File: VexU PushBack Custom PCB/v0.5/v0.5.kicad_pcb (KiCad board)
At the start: 2 copper layers, 40.5 x 70 mm, 40 parts, among them J1 4P4C, J2 Conn_01x04_Pin, U1 Teensy4.1, U2 MP2338GTL-P, U3 4069, U4 MAX485E

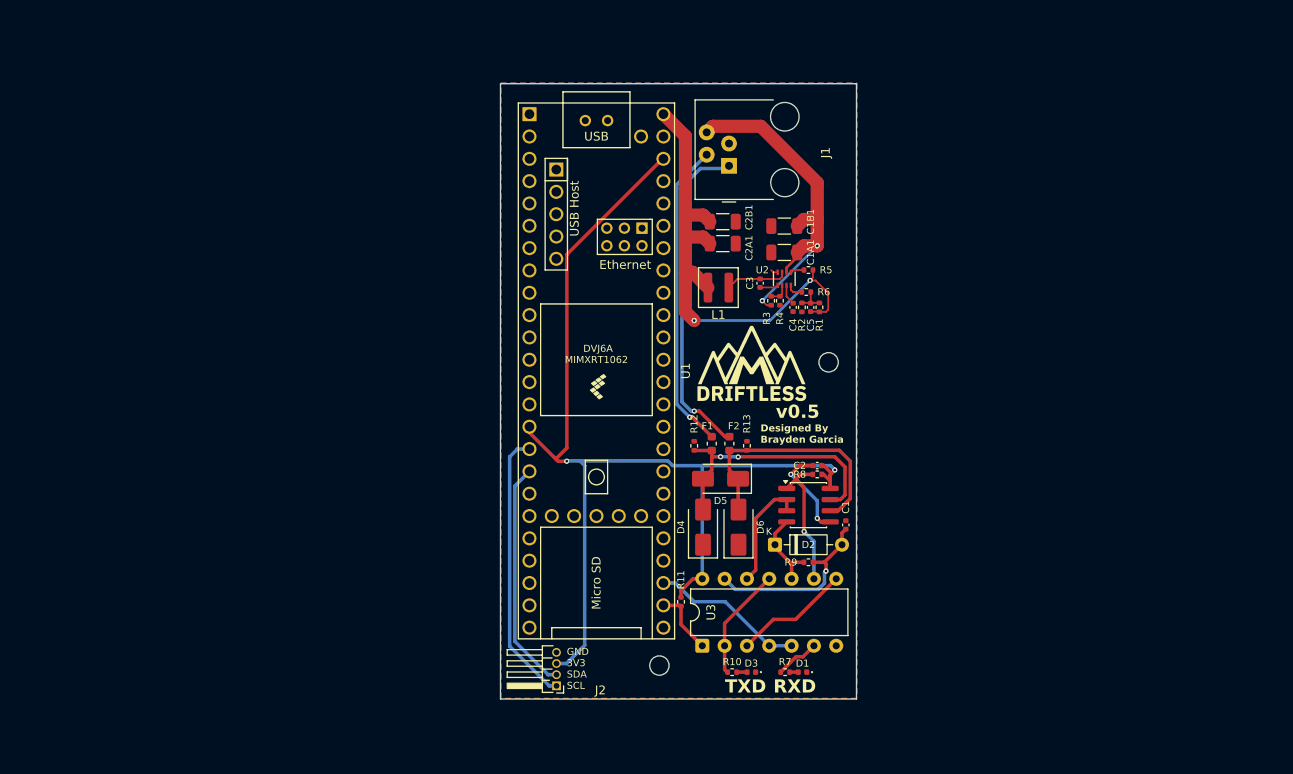
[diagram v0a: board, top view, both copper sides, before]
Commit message: Schematic fully done
will need to keep working on tracing and component layout
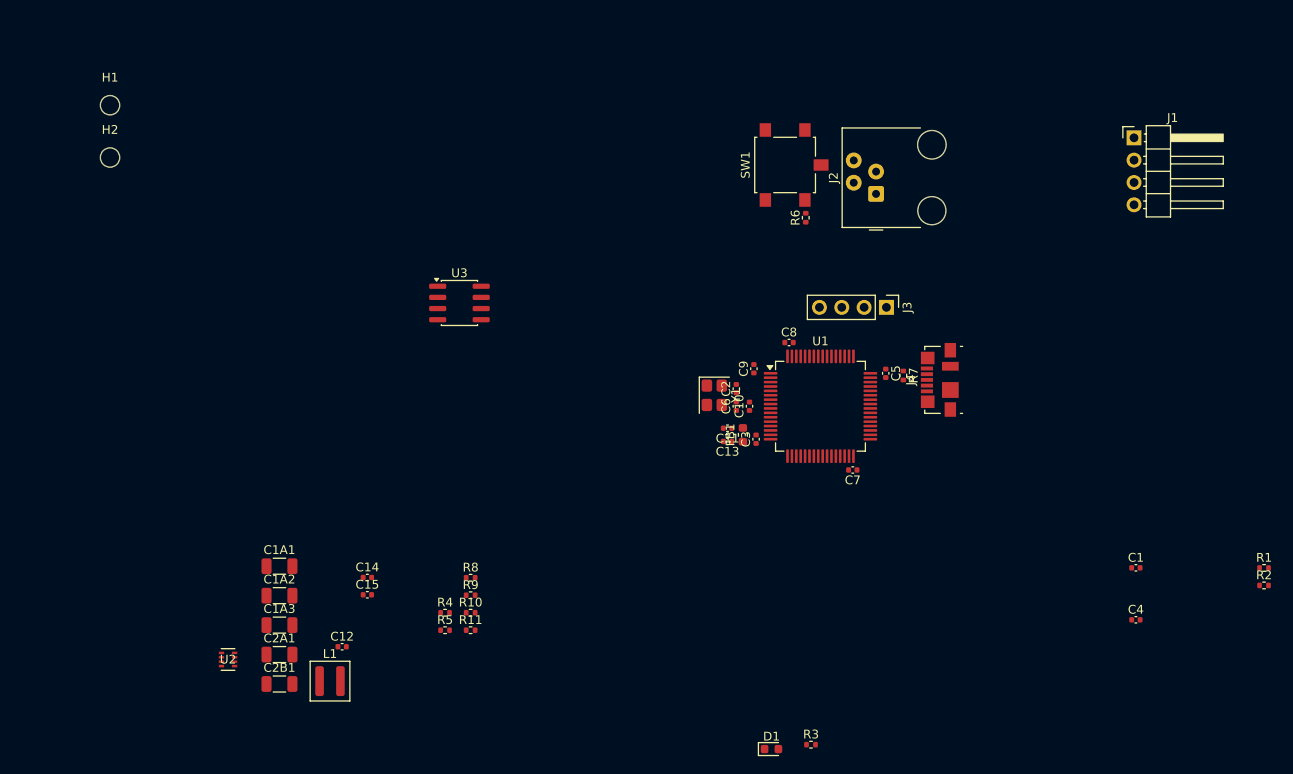
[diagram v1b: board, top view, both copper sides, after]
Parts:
- removed C1B1: 0.1μF, Capacitor_SMD:C_1206_3216Metric
- removed D2: 1N4148, Diode_THT:D_DO-35_SOD27_P7.62mm_Horizontal
- removed D3: TXD, LED_SMD:LED_0402_1005Metric
- removed D4, D5, D6: SMAJ6.5CA, Diode_SMD:D_SMA
- removed F1, F2: 0.3A, Fuse:Fuse_0603_1608Metric
- removed G***: LOGO, LOGO
- removed R12, R13: 4.7k, Resistor_SMD:R_0402_1005Metric
- removed U4: MAX485E, Package_SO:SOIC-8_3.9x4.9mm_P1.27mm
- added C10: 10n, Capacitor_SMD:C_0402_1005Metric, F.Cu at (113.5, 60.5)
- added C11: 1u, Capacitor_SMD:C_0402_1005Metric, F.Cu at (111.0, 63.0)
- added C12: 22nF, Capacitor_SMD:C_0402_1005Metric, F.Cu at (67.2, 87.9)
- added C13: 1u, Capacitor_SMD:C_0402_1005Metric, F.Cu at (111.0, 64.5)
- added C14: 0.1μF, Capacitor_SMD:C_0402_1005Metric, F.Cu at (70.0, 80.0)
- added C15: 470pF, Capacitor_SMD:C_0402_1005Metric, F.Cu at (70.0, 82.0)
- added C1A2: 10u, Capacitor_SMD:C_1206_3216Metric, F.Cu at (60.0, 82.0)
- added C1A3: 0.1μF, Capacitor_SMD:C_1206_3216Metric, F.Cu at (60.0, 85.4)
- added C6: 10p, Capacitor_SMD:C_0402_1005Metric, F.Cu at (112.0, 60.5)
- added C7: 100n, Capacitor_SMD:C_0402_1005Metric, F.Cu at (125.2, 67.8)
- added C8: 100n, Capacitor_SMD:C_0402_1005Metric, F.Cu at (118.0, 53.2)
- added C9: 100n, Capacitor_SMD:C_0402_1005Metric, F.Cu at (114.0, 56.2)
- added FB1: 120R, Inductor_SMD:L_0603_1608Metric, F.Cu at (112.8, 63.8)
- added J3: Conn_01x04_Pin, Connector_PinHeader_2.54mm:PinHeader_1x04_P2.54mm_Vertical, F.Cu at (129.1, 49.2)
- added J4: USB_B_Micro, Connector_USB:USB_Micro-B_Molex_47346-0001, F.Cu at (135.2, 57.5)
- added SW1: SW_SPDT, Button_Switch_SMD:SW_SPST_B3S-1100, F.Cu at (118.5, 33.0)
- added Y1: 16MHz, Crystal:Crystal_SMD_3225-4Pin_3.2x2.5mm, F.Cu at (109.5, 59.2)
- C1: value 100pF -> 10u
- C1A1: value 22μF -> 10u
- C2: value 0.1uF -> 10p
- C3: value 0.1μF -> 100n
- C4: value 22nF -> 100n
- C5: value 300pF -> 100n
- D1: value RXD -> RED; footprint LED_SMD:LED_0402_1005Metric -> LED_SMD:LED_0603_1608Metric
- J1: value 4P4C -> Conn_01x04_Pin; footprint Connector_RJ:RJ9_Evercom_5301-440xxx_Horizontal -> Connector_PinHeader_2.54mm:PinHeader_1x04_P2.54mm_Horizontal
- J2: value Conn_01x04_Pin -> 4P4C; footprint Connector_PinHeader_1.27mm:PinHeader_1x04_P1.27mm_Horizontal -> Connector_RJ:RJ9_Evercom_5301-440xxx_Horizontal
- R1: value 90.9kΩ -> 1.5k
- R10: value 2.4k -> 9.09kΩ
- R11: value 4.7k -> 51kΩ
- R2: value 10kΩ -> 1.5k
- R3: value 191kΩ -> 1.5k
- R4: value 49.9kΩ -> 191kΩ
- R5: value 10kΩ -> 49.9kΩ
- R6: value 10kΩ -> 10k
- R7: value 2.4k -> 1.5k
- R8: value 4.7k -> 100kΩ
- R9: value 56k -> 10kΩ
- U1: value Teensy4.1 -> STM32G431RBT6; footprint teensy.pretty-master:Teensy41 -> Package_QFP:LQFP-64_10x10mm_P0.5mm
- U3: value 4069 -> MAX485E; footprint Package_DIP:DIP-14_W7.62mm -> Package_SO:SOIC-8_3.9x4.9mm_P1.27mm
- moved H1 86.8 mm to (40.8, 26.2), turned to 0 degrees
- moved H2 85.1 mm to (40.8, 32.2), turned to 0 degrees
- moved U2 76.7 mm to (54.2, 89.3), turned to 0 degrees
- moved C2B1 72.9 mm to (60.0, 92.1)
- moved C2A1 68.8 mm to (60.0, 88.8)
- moved C1A1 67.6 mm to (60.0, 78.7), turned to 0 degrees
- moved J2 66.7 mm to (127.9, 36.3), turned to 90 degrees
- moved L1 62.9 mm to (65.8, 91.8), turned to 0 degrees
- moved R2 61.4 mm to (172.0, 80.9), turned to 0 degrees
- moved R1 58.6 mm to (172.0, 78.9), turned to 0 degrees
- moved R5 58.2 mm to (78.9, 86.0)
- moved C4 52.8 mm to (157.5, 84.8), turned to 0 degrees
- moved R4 52.1 mm to (78.9, 84.0), turned to 0 degrees
- moved R3 50.7 mm to (120.5, 99.0), turned to 0 degrees
- moved U3 47.8 mm to (80.5, 48.8), turned to 0 degrees
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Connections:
- C1 pad 1: Net-(D2-A) -> +3V3
- C1A1 pad 1: 12V -> VBUS
- C2 pad 1: 3V3 -> /HSE_IN
- C2A1 pad 1: 5V -> +3V3
- C2B1 pad 1: 5V -> +3V3
- C3 pad 1: Net-(U2-BST) -> +3V3
- C3 pad 2: Net-(U2-SW) -> GND
- C4 pad 1: Net-(U2-SS) -> /NRST
- C5 pad 1: Net-(C5-Pad1) -> +3V3
- C5 pad 2: 5V -> GND
- D1 pad 1: GND -> Net-(D1-K)
- D1 pad 2: Net-(D1-A) -> +3V3
- J1 pad 1: A -> GND
- J1 pad 2: B -> +3V3
- J1 pad 3: GND -> /I2C3_SDA
- J1 pad 4: 12V -> /I2C3_SCL
- J2 pad 1: SCL -> A
- J2 pad 2: SDA -> B
- J2 pad 3: 3V3 -> GND
- J2 pad 4: GND -> VBUS
- L1 pad 2: 5V -> +3V3
- R1 pad 1: Net-(C5-Pad1) -> +3V3
- R1 pad 2: 5V -> /I2C3_SDA
- R10 pad 1: Net-(R10-Pad1) -> GND
- R10 pad 2: Net-(D3-A) -> Net-(C15-Pad1)
- R11 pad 1: 3V3 -> Net-(C15-Pad1)
- R11 pad 2: RXD -> +3V3
- R2 pad 1: GND -> +3V3
- R2 pad 2: Net-(C5-Pad1) -> /I2C3_SCL
- R3 pad 1: 12V -> Net-(D1-K)
- R3 pad 2: Net-(U2-EN) -> GND
- R4 pad 1: Net-(U2-EN) -> VBUS
- R4 pad 2: GND -> Net-(U2-EN)
- R5 pad 1: Net-(U2-PG) -> Net-(U2-EN)
- R5 pad 2: 5V -> GND
- R6 pad 1: Net-(U2-FB) -> /BOOT0
- R6 pad 2: Net-(C5-Pad1) -> /SW_BOOT0
- R7 pad 1: Net-(R7-Pad1) -> +3V3
- R7 pad 2: Net-(D1-A) -> /USB_D+
- R8 pad 1: Net-(U4-RO) -> Net-(U2-PG)
- R8 pad 2: 3V3 -> +3V3
- R9 pad 1: Net-(D2-K) -> Net-(U2-FB)
- R9 pad 2: Net-(D2-A) -> Net-(C15-Pad1)
- U1 pad 1: GND -> +3V3
- U1 pad 15: 3V3 -> GND
- U1 pad 16: SCL -> +3V3
- U1 pad 17: SDA -> unconnected-(U1-PA3-Pad17)
- U1 pad 26: RXD -> unconnected-(U1-PB2-Pad26)
- U1 pad 27: TXD -> GND
- U1 pad 29: unconnected-(U1-37_CS-Pad29) -> +3.3VA
- U1 pad 31: unconnected-(U1-39_MISO1_OUT1A-Pad31) -> GND
- U1 pad 32: unconnected-(U1-40_A16-Pad32) -> +3V3
- U1 pad 34: GND -> unconnected-(U1-PB12-Pad34)
- U1 pad 40: unconnected-(U1-18_A4_SDA-Pad40) -> /I2C3_SCL
- U1 pad 41: unconnected-(U1-19_A5_SCL-Pad41) -> /I2C3_SDA
- U1 pad 45: unconnected-(U1-23_A9_CRX1_MCLK1-Pad45) -> /USB_D-
- U1 pad 46: 3V3 -> /USB_D+
- U1 pad 48: 5V -> +3V3
- U1 pad 49: unconnected-(U1-VUSB-Pad49) -> /SWDIO
- U1 pad 5: unconnected-(U1-3_LRCLK2-Pad5) -> /HSE_IN
- U1 pad 50: unconnected-(U1-VBAT-Pad50) -> /SWCLK
- U1 pad 58: unconnected-(U1-GND-Pad58) -> TX_EN
- U1 pad 59: unconnected-(U1-GND-Pad59) -> TXD
- U1 pad 6: unconnected-(U1-4_BCLK2-Pad6) -> /HSE_OUT
- U1 pad 60: unconnected-(U1-R+-Pad60) -> RXD
- U1 pad 61: unconnected-(U1-LED-Pad61) -> /BOOT0
- U1 pad 63: unconnected-(U1-T+-Pad63) -> GND
- U1 pad 64: unconnected-(U1-GND-Pad64) -> +3V3
- U1 pad 7: unconnected-(U1-5_IN2-Pad7) -> /NRST
- U2 pad 2: 12V -> VBUS
- U3 pad 2: Net-(R10-Pad1) -> TX_EN
- U3 pad 3: Net-(U3-Pad3) -> TX_EN
- U3 pad 5: TXD -> GND
- U3 pad 6: Net-(R7-Pad1) -> A
- U3 pad 7: GND -> B
- U3 pad 8: Net-(U3-Pad3) -> +3.3V
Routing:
- net 3V3: track 123.5 -> 0.00 mm, vias 2 -> 0
- net 5V: track 57.4 -> 0.00 mm, vias 2 -> 0
- net 12V: track 40.9 -> 0.00 mm, vias 2 -> 0
- net A: track 37.8 -> 0.00 mm, vias 1 -> 0
- net B: track 35.3 -> 0.00 mm, vias 1 -> 0
- net SCL: track 31.4 -> 0.00 mm
- net Net-(D4-A2): track 30.0 -> 0.00 mm, vias 2 -> 0
- net Net-(D5-A1): track 28.6 -> 0.00 mm
- net SDA: track 26.3 -> 0.00 mm
- net Net-(D2-A): track 20.8 -> 0.00 mm, vias 1 -> 0
- net TXD: track 17.5 -> 0.00 mm
- net Net-(U4-RO): track 15.8 -> 0.00 mm, vias 1 -> 0
- net Net-(U3-Pad3): track 13.3 -> 0.00 mm
- net Net-(U4-DE): track 13.0 -> 0.00 mm
- net Net-(R10-Pad1): track 12.9 -> 0.00 mm
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- removed copper zone on B.Cu, net GND
- removed copper zone on F.Cu, net GND
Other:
- board outline removed
- board text removed: "Designed By Brayden Garcia"
- board text removed: "GND 3V3 SDA SCL"
- board text removed: "RXD"
- board text removed: "TXD"
- board text removed: "v0.5"

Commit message: Layout of buck convertr
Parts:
- moved C4 130.9 mm to (32.4, 46.0), turned to 90 degrees
- moved C1 129.8 mm to (32.4, 44.0), turned to -90 degrees
- moved J1 94.6 mm to (66.0, 54.9)
- moved R3 80.9 mm to (77.5, 30.5), turned to 90 degrees
- moved D1 78.7 mm to (80.0, 29.5), turned to 180 degrees
- moved SW1 76.0 mm to (42.6, 37.5)
- moved H1 73.8 mm to (102.0, 67.5)
- moved H2 73.8 mm to (102.0, 73.5)
- moved R6 70.5 mm to (49.4, 38.5)
- moved C10 69.8 mm to (44.4, 50.5)
- moved C11 69.8 mm to (41.9, 53.0)
- moved C13 69.8 mm to (41.9, 54.5)
- moved C2 69.8 mm to (42.9, 48.5)
- moved C3 69.8 mm to (45.2, 54.2)
- moved C5 69.8 mm to (59.9, 46.8)
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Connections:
- D1 pad 1: Net-(D1-K) -> GND
- D1 pad 2: +3V3 -> Net-(D1-A)
- R3 pad 1: Net-(D1-K) -> +3V3
- R3 pad 2: GND -> Net-(D1-A)

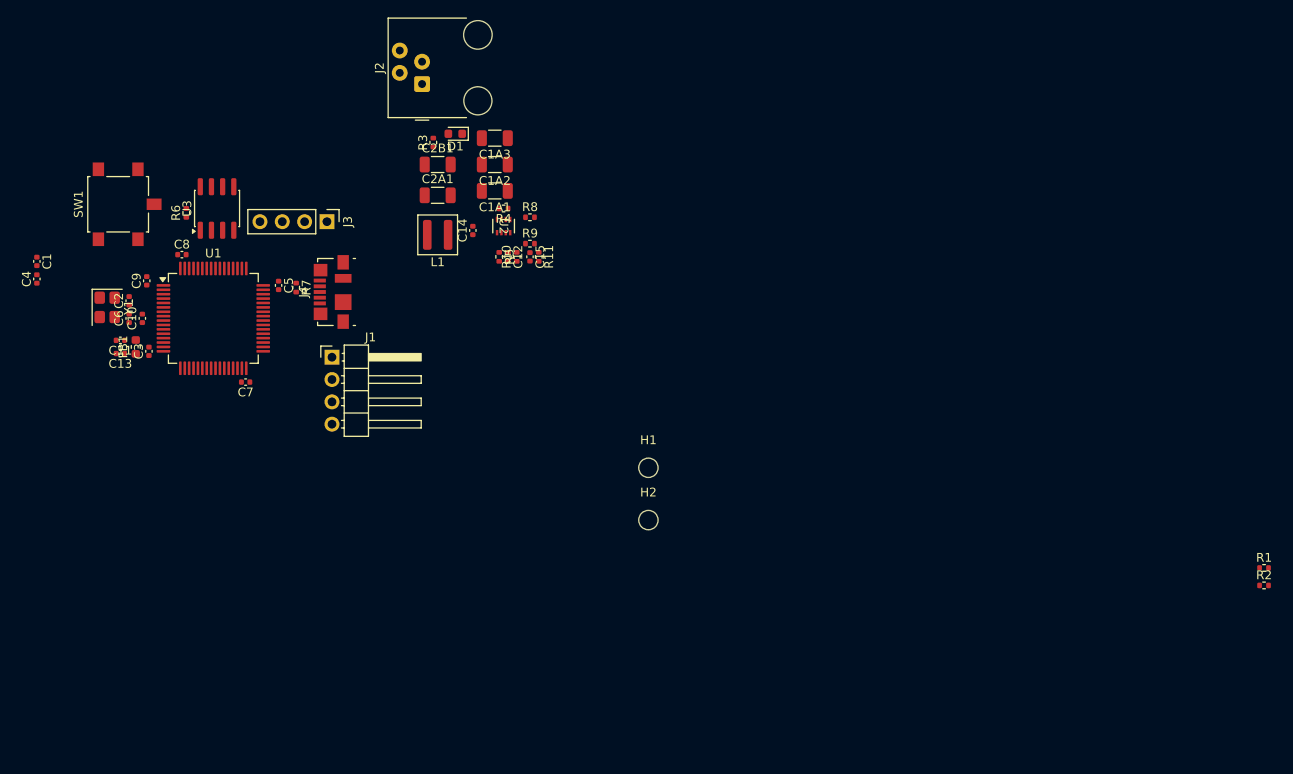
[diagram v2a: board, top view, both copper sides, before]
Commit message: Different Partial Layout Design
Still have to do tracing and finishing layout
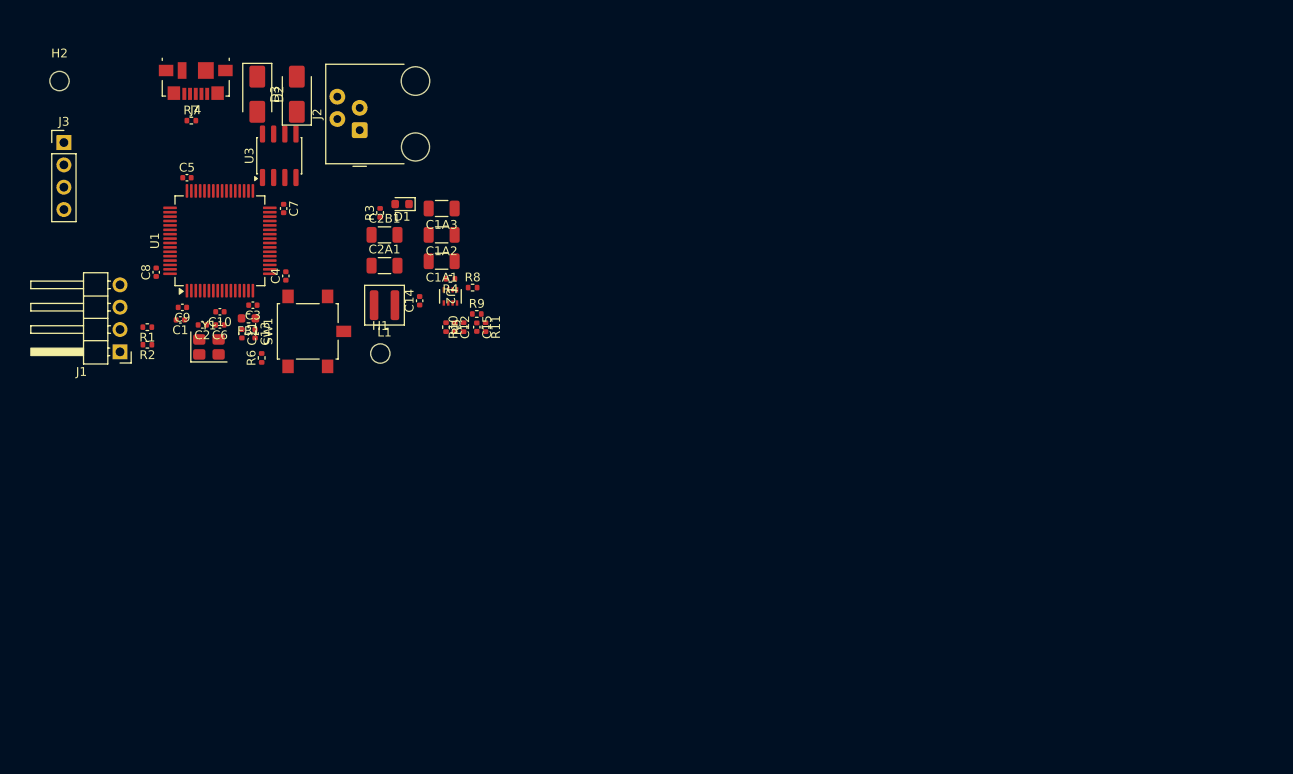
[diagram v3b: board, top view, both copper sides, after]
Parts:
- added D2: SMAJ6.5CA, Diode_SMD:D_SMA, F.Cu at (57.5, 25.0)
- added D3: SMAJ6.5CA, Diode_SMD:D_SMA, F.Cu at (62.0, 25.0)
- moved R1 130.0 mm to (45.0, 51.5), turned to 180 degrees
- moved R2 130.0 mm to (45.0, 53.5), turned to 180 degrees
- moved H2 83.6 mm to (35.0, 23.5)
- moved H1 33.2 mm to (71.5, 54.5)
- moved J3 31.2 mm to (35.5, 30.5), turned to 0 degrees
- moved J4 28.6 mm to (50.5, 23.5), turned to 180 degrees
- moved C4 28.3 mm to (60.8, 45.7)
- moved SW1 26.0 mm to (64.2, 52.0)
- moved J1 24.1 mm to (41.9, 54.3), turned to 180 degrees
- moved R7 22.4 mm to (50.0, 28.0), turned to 0 degrees
- moved C7 20.2 mm to (60.5, 38.0), turned to -90 degrees
- moved R6 18.6 mm to (58.0, 55.0)
- moved C1 17.6 mm to (48.8, 50.7), turned to 180 degrees
- moved C5 16.1 mm to (49.5, 34.5), turned to 0 degrees
- moved C13 15.5 mm to (57.2, 52.2), turned to -90 degrees
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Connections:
- J1 pad 1: GND -> /I2C3_SCL
- J1 pad 2: +3V3 -> /I2C3_SDA
- J1 pad 3: /I2C3_SDA -> +3V3
- J1 pad 4: /I2C3_SCL -> GND

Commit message: Layout redesign for tigher component placing
Changed switch sized and mad layout smaler
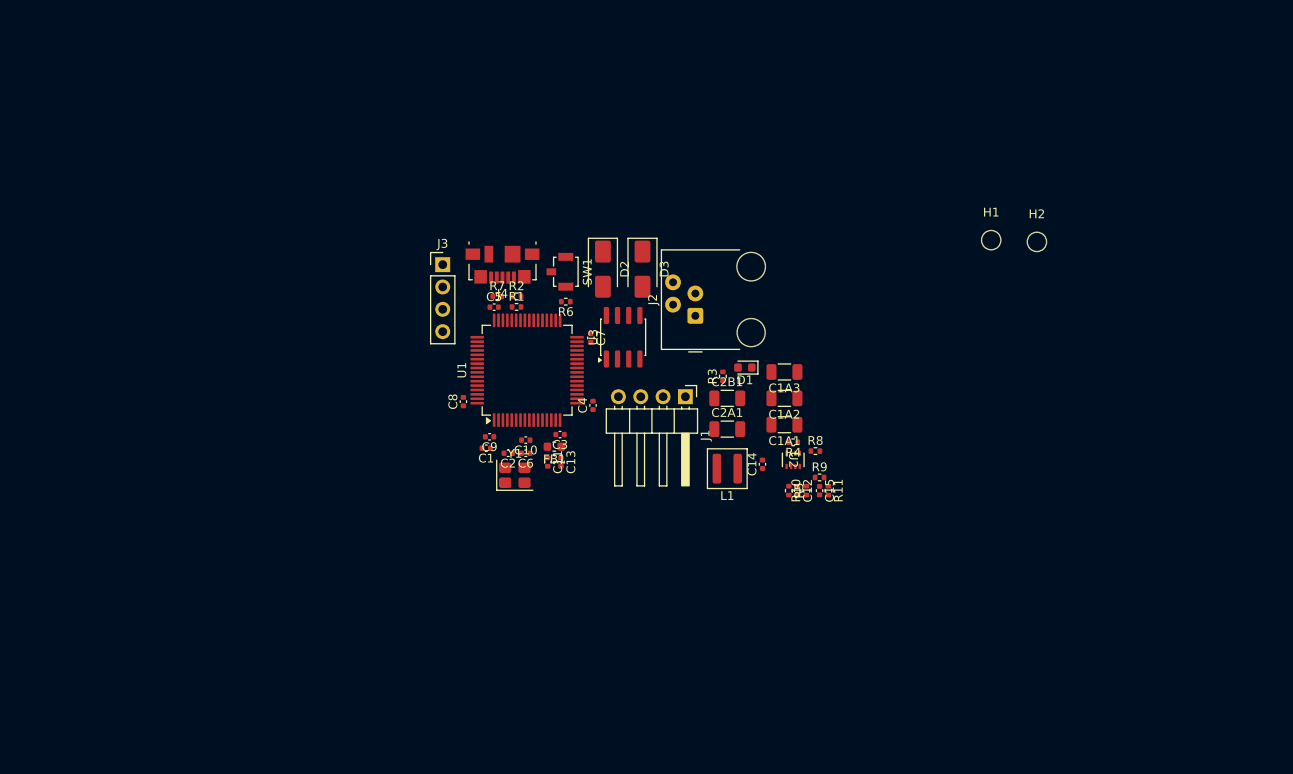
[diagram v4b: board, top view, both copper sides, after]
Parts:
- SW1: footprint Button_Switch_SMD:SW_SPST_B3S-1100 -> Button_Switch_SMD:SW_SPST_B3U-1100P
- moved H2 112.7 mm to (146.2, 41.8)
- moved H1 70.7 mm to (141.0, 41.6)
- moved J1 64.5 mm to (106.2, 59.4), turned to -90 degrees
- moved J3 45.3 mm to (78.6, 44.4)
- moved U3 44.2 mm to (99.1, 52.6)
- moved D2 44.1 mm to (96.8, 44.9)
- moved D3 44.1 mm to (101.3, 44.9), turned to -90 degrees
- moved J2 43.6 mm to (107.3, 50.2)
- moved C12 43.2 mm to (119.0, 70.1)
- moved C14 43.2 mm to (115.0, 67.1)
- moved C15 43.2 mm to (121.5, 70.1)
- moved C1A1 43.2 mm to (117.5, 62.6)
- moved C1A2 43.2 mm to (117.5, 59.6)
- moved C1A3 43.2 mm to (117.5, 56.6)
- moved C2A1 43.2 mm to (111.0, 63.1)
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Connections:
- D3 pad 1: A -> GND
- D3 pad 2: GND -> A
